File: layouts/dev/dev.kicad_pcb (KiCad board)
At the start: 6 copper layers, 32.5 x 59.6 mm, 92 parts

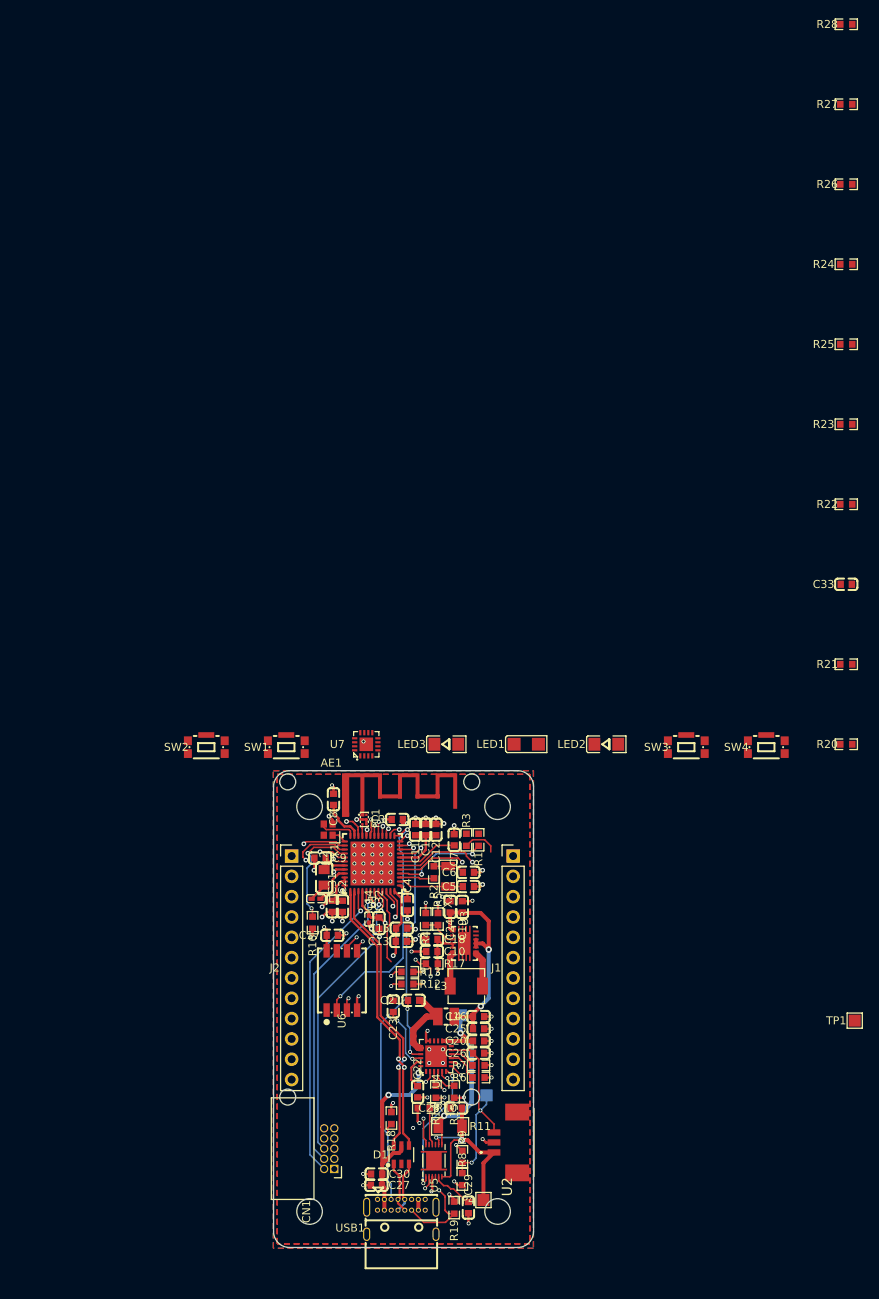
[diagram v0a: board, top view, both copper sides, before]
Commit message: feat: cut the expander load to two LEDs and one button
Three LEDs and two buttons measured 166.5 mm2 of courtyard and did not fit
the board's free pockets. Two LEDs and one button do. The expander stays -
on a dev board the eight ports are worth having, the part is cheap, and
these boards are hand-assembled so JLCPCB's extended-part feeder fee never
applies.

Seven parts leave the board: one LED with its resistor, one button with its
pull-up, and the three spare pull-downs. 92 footprints down to 85.

The five unused ports now carry no resistors at all, which the datasheet
sanctions explicitly: "Resistors are required for inputs (on P-port) that
may float ... Outputs (in the P-port) do not need pull-up resistors." Five
0603 parts is 21.5 mm2 spent on nothing; one line in the init routine costs
none. This is a contract with the firmware and it is written down, because
it has a price: until the configuration register is first written those
pins float, and a floating CMOS input draws up to about 100 uA. Five of
them is half a milliamp - nothing for the milliseconds before the program
starts, a real drain on a board left in a drawer with a cell attached.

While doing this, a worse variant of an earlier bug surfaced. Zones hold
their net by number, atopile renumbers on every build, and the unconnected
expander ports had been given nets named after their pin numbers. Three
ground pours ended up pointing at net "7" - port P7 of the expander - and
the power plane at "5". The earlier failure left zones with an empty name,
which is visible; this one gave them a real net that happened to belong to
something else, which is not.

Fixed at both ends. Every pin that leads nowhere now has a name
(EXP_P3_NC..EXP_P7_NC, SD_DAT1_NC, SD_DAT2_NC, AT0_NC, AT1_NC), so no
number can masquerade as a net. And board_setup's guard now treats an
all-digits zone net as lost, not just an empty one: on inner layers the
layer map is the source of truth, while on outer layers it repairs only
what cle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
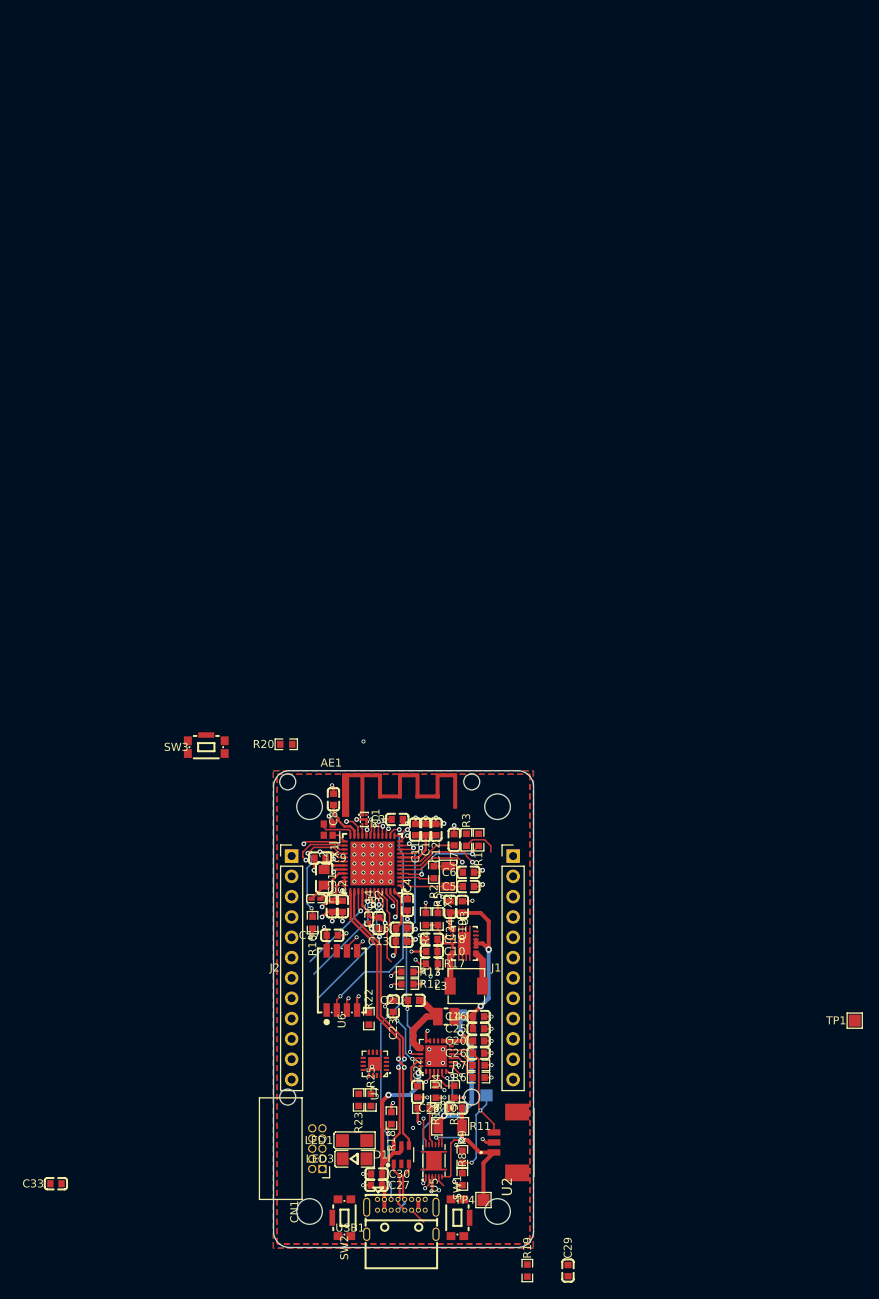
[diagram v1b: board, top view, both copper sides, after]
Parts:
- removed LED2: , Foshan_NationStar_Optoelectronics_NCD1206R1:LED1206-R-RD_RED
- removed R21, R26, R27, R28: 10kΩ ±1%, YAGEO_RC0603FR_0710KL:R0603
- removed R24: 1kΩ ±1%, UNI_ROYAL_0603WAF1001T5E:R0603
- removed SW4: , C_K_KMR221GLFS:KEY-SMD_KMR2XXGXXX
- moved C33 124.0 mm to (-18.8, 54.9)
- moved R25 111.6 mm to (20.6, 44.5), turned to -90 degrees
- moved R23 104.1 mm to (19.1, 44.5), turned to 90 degrees
- moved R22 87.7 mm to (20.3, 34.3), turned to -90 degrees
- moved R20 70.0 mm to (10.0, 0.00)
- moved SW1 63.1 mm to (31.8, 59.2), turned to -90 degrees
- moved SW2 61.5 mm to (16.9, 59.2), turned to 90 degrees
- moved SW3 60.0 mm to (0.00, 0.00)
- moved LED1 54.0 mm to (18.5, 49.5)
- moved LED3 53.1 mm to (18.5, 51.8)
- moved U7 40.0 mm to (21.1, 40.0), turned to 90 degrees
- moved C29 14.7 mm to (45.2, 65.8)
- moved R19 12.1 mm to (40.1, 65.8), turned to -90 degrees
- moved CN1 1.49 mm to (13.9, 50.5)
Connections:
- net 1 renamed SD_DAT2_NC
- net 26 renamed AT0_NC
- net 27 renamed AT1_NC
- net 7 renamed SD_DAT1_NC
- R20 pad 2: BTN_USR0 -> BTN_USR
- SW3 pad 1: BTN_USR0 -> BTN_USR
- SW3 pad 2: BTN_USR0 -> BTN_USR
- U7 pad 1: 10 -> +3V3
- U7 pad 10: EXP_LED1 -> EXP_P7_NC
- U7 pad 11: EXP_LED2 -> EXP_INT
- U7 pad 12: BTN_USR0 -> PMIC_SCL
- U7 pad 13: GND -> PMIC_SDA
- U7 pad 14: BTN_USR1 -> +3V3
- U7 pad 15: 8 -> +3V3
- U7 pad 16: +3V3 -> GND
- U7 pad 2: EXP_INT -> EXP_LED0
- U7 pad 3: PMIC_SCL -> EXP_LED1
- U7 pad 4: PMIC_SDA -> BTN_USR
- U7 pad 5: +3V3 -> EXP_P3_NC
- U7 pad 6: +3V3 -> GND
- U7 pad 7: GND -> EXP_P4_NC
- U7 pad 8: 9 -> EXP_P5_NC
- U7 pad 9: EXP_LED0 -> EXP_P6_NC
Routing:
- net SWDIO: track 38.2 -> 11.6 mm
- net SWCLK: track 36.8 -> 13.2 mm
- net SWO: track 35.9 -> 16.8 mm
- net CC2: track 59.9 -> 51.6 mm
- net GAUGE_VDD_1V8: track 5.31 -> 1.37 mm
- net GND: track 63.6 -> 62.4 mm, vias 78 -> 77
- net EXP_P4_NC: vias 0 -> 1

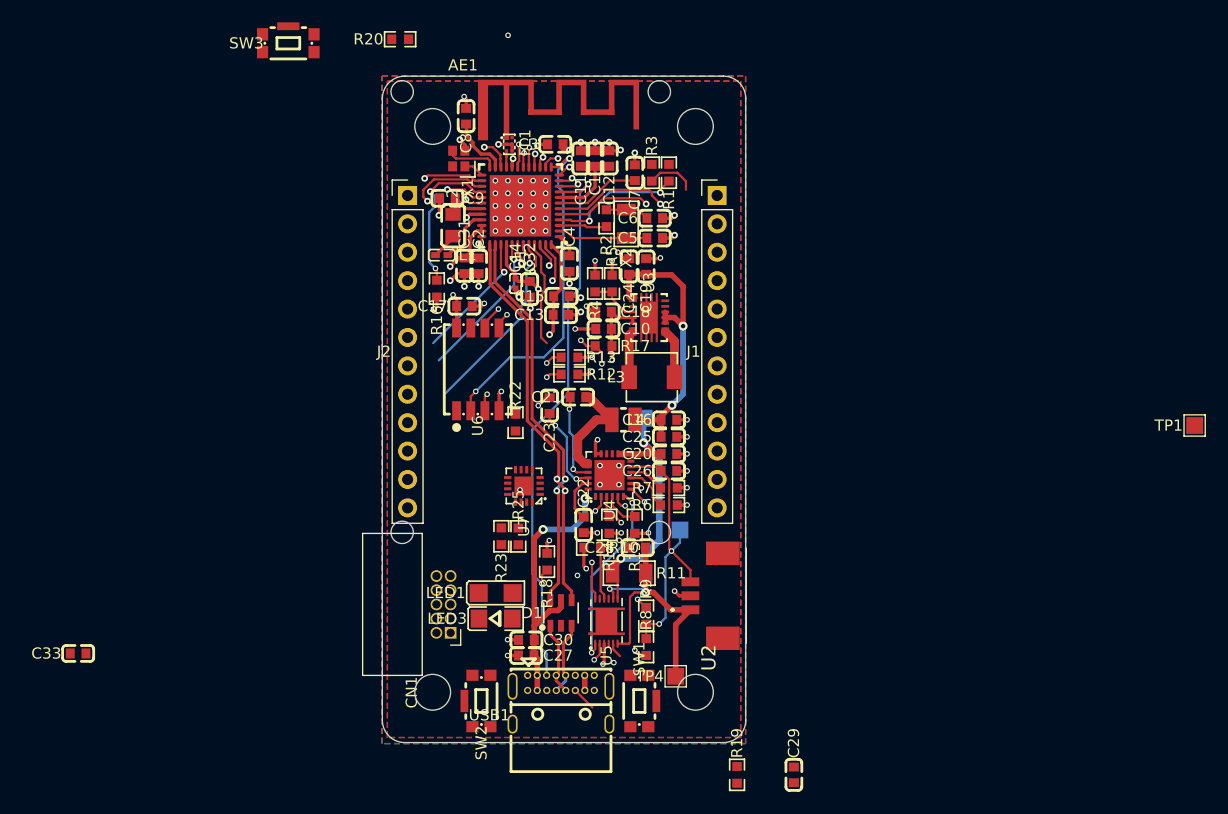
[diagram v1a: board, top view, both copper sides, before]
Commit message: feat: bring the hand-reworked headers and mounting holes into the source
Layout work in pcbnew moved the signals around on both headers, brought
three spare expander ports out, relocated the M3 holes and deleted the
inherited 2.0 mm set. The source now describes exactly that, so the next
ato build reproduces it instead of reverting it.

Headers:

  J2 (left)   1 SD_CLK  2 PA9   3 PA10   4 GND   5 EXT_CS  6 SD_MISO
              7 GND     8 SD_MOSI  9 GND  10 EXP_P4  11 EXP_P5  12 EXP_P6
  J1 (right)  1 +3V3    2 PA3   3 PA8    4 PMIC_SCL  5 GND   6 PMIC_SDA
              7 PB6     8 PB7   9 PA2   10 +3V3   11 GND   12 BOOT0

The left strip has no supply rail any more, only ground; +3V3 moved wholly
to the right, where it sits on two positions with two grounds, because a
single pair on a twelve-way strip means a long return for anything powered
from the side. VBUS and SYS left the headers entirely - both nets are still
on the board, they just do not reach goldpins.

EXP_P4..P6 lost their _NC suffix. The suffix existed to stop atopile naming
those nets after pin numbers, where a numeric name can collide with the
numbering zones point at; now they lead to a header, so the name would be a
lie. Their copper survived the rename - eight elements each, before and
after.

Mounting holes: MOUNT_EDGE_MM 4.5 -> 3.5, because at 4.5 the screw heads
ate space the parts needed. The laminate web drops from 2.90 to 1.90 mm,
still six times the threshold. The inherited 2.0 mm set is gone along with
its constants; it existed so the board would fit old brackets, and no
bracket is worth pushing the outline around. If it ever returns it returns
from git history, not from dead code.

Three things were caught before they could do damage. AT0 and AT1 had been
routed to J2 - ST's own pin data types both as NC, so they are not
application pins at all - and SD_CLK and PA9 had dropped off the strips,
leaving an SPI header without a clock and a UART without a transmitter. All
three were fixed by 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
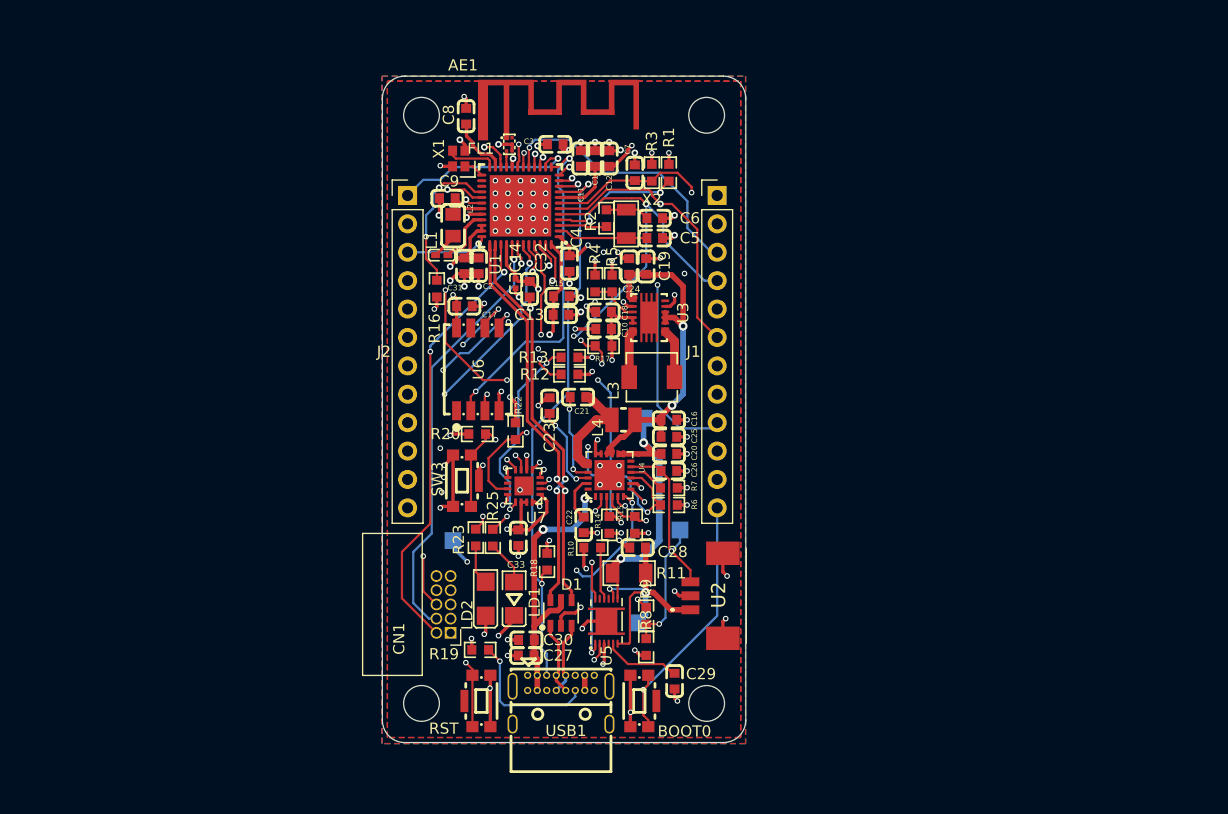
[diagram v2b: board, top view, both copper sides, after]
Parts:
- TP1, TP4: moved to B.Cu
- moved TP1 67.1 mm to (14.7, 44.8), turned to -90 degrees
- moved SW3 42.6 mm to (15.9, 39.5), turned to -90 degrees
- moved C33 40.7 mm to (20.6, 44.6), turned to -90 degrees
- moved R20 36.0 mm to (16.9, 35.3)
- moved R19 25.5 mm to (17.2, 54.6), turned to 180 degrees
- moved C29 13.6 mm to (34.5, 57.4)
- moved TP4 5.86 mm to (31.2, 52.2), turned to 180 degrees
- moved LED3 2.43 mm to (20.2, 50.0), turned to 90 degrees
- moved R23 2.29 mm to (16.8, 44.6), turned to -90 degrees
- moved R25 2.29 mm to (18.3, 44.6)
- moved LED1 1.02 mm to (17.7, 50.0), turned to 90 degrees
- moved R22 0.76 mm to (20.3, 35.1)
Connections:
- J1 pad 10: PB7 -> +3V3
- J1 pad 12: GND -> BOOT0
- J1 pad 2: PA2 -> PA3
- J1 pad 3: PA3 -> PA8
- J1 pad 4: PA8 -> PMIC_SCL
- J1 pad 5: PA9 -> GND
- J1 pad 6: PA10 -> PMIC_SDA
- J1 pad 7: PMIC_SCL -> PB6
- J1 pad 8: PMIC_SDA -> PB7
- J1 pad 9: PB6 -> PA2
- J2 pad 1: VBUS -> SD_CLK
- J2 pad 10: GND -> EXP_P4
- J2 pad 11: BOOT0 -> EXP_P5
- J2 pad 12: GND -> EXP_P6
- J2 pad 2: SYS -> PA9
- J2 pad 3: +3V3 -> PA10
- J2 pad 5: SD_CLK -> EXT_CS
- J2 pad 9: EXT_CS -> GND
- U7 pad 7: EXP_P4_NC -> EXP_P4
- U7 pad 8: EXP_P5_NC -> EXP_P5
- U7 pad 9: EXP_P6_NC -> EXP_P6
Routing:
- net NRST: track 12.0 -> 97.8 mm, vias 0 -> 2
- net BOOT0: track 12.0 -> 83.7 mm, vias 2 -> 4
- net PMIC_SCL: track 28.0 -> 93.3 mm, vias 4 -> 6
- net PMIC_SDA: track 28.8 -> 89.7 mm, vias 4 -> 6
- net CHG_STAT: track 5.33 -> 53.0 mm, vias 1 -> 4
- net CHG_CE: track 7.67 -> 49.1 mm, vias 1 -> 3
- net GND: track 62.4 -> 101.7 mm, vias 77 -> 97
- net CHG_PG: track 4.72 -> 42.3 mm, vias 2 -> 4
- net PA2: track 1.24 -> 33.1 mm, vias 1 -> 2
- net SWDIO: track 11.6 -> 39.9 mm, vias 1 -> 2
- net SWCLK: track 13.2 -> 38.5 mm
- net +3V3: track 55.9 -> 79.9 mm, vias 13 -> 20
- net PA8: track 1.75 -> 24.5 mm
- net PB6: track 2.34 -> 23.4 mm, vias 1 -> 2
- net SWO: track 16.8 -> 36.9 mm, vias 1 -> 3
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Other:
- outline, holes or cut-outs redrawn
- board text added: "+3V3"
- board text added: "AT0_NC"
- board text added: "AT1_NC"
- board text added: "BOOT0"
- board text added: "EXP_P4"
- board text added: "EXP_P5"
- board text added: "EXP_P6"
- board text added: "EXT_CS"
- board text added: "GND"
- board text added: "LD1"
- board text added: "LD2"
- board text added: "PA10"
- board text added: "PA2"
- board text added: "PA3"
- board text added: "PA8"
- board text added: "PB6"
- board text added: "PB7"
- board text added: "RST"
- board text added: "SCL"
- board text added: "SDA"
- board text added: "SD_MISO"
- board text added: "SD_MOSI"
